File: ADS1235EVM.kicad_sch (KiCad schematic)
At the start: 60 parts, among them J1 Conn_01x04_Pin, J2 Conn_01x11_Pin, U1 ADS1235QWRHMRQ1, U2 LM27762, U5 UCC27524DGN

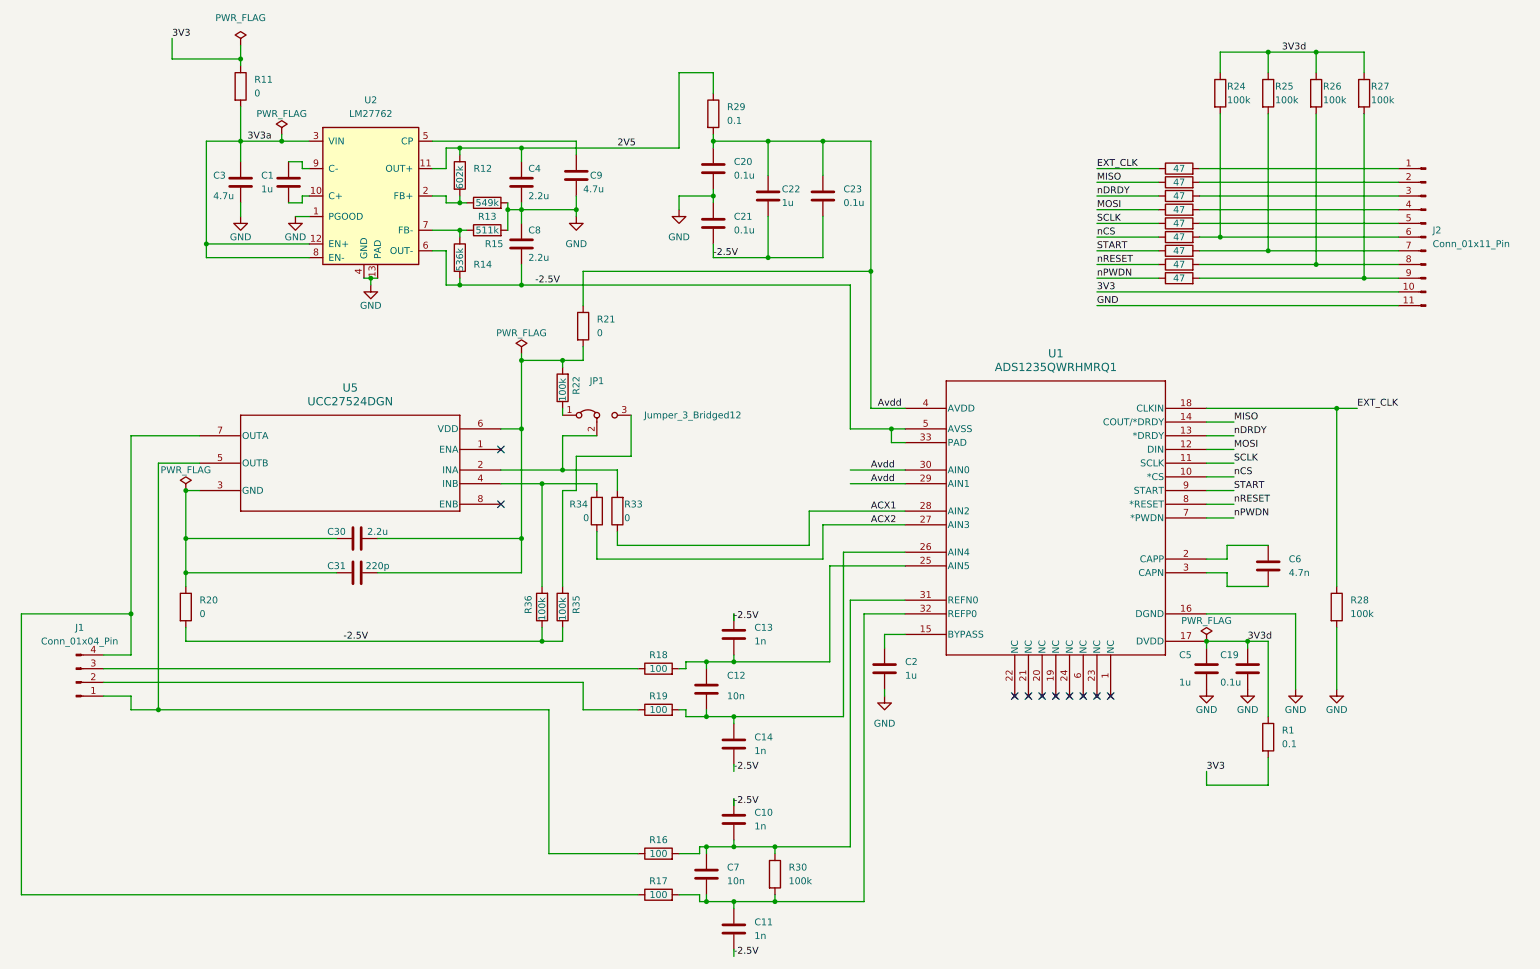
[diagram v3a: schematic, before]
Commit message: Add of 2.54mm SPI connector & open jumper
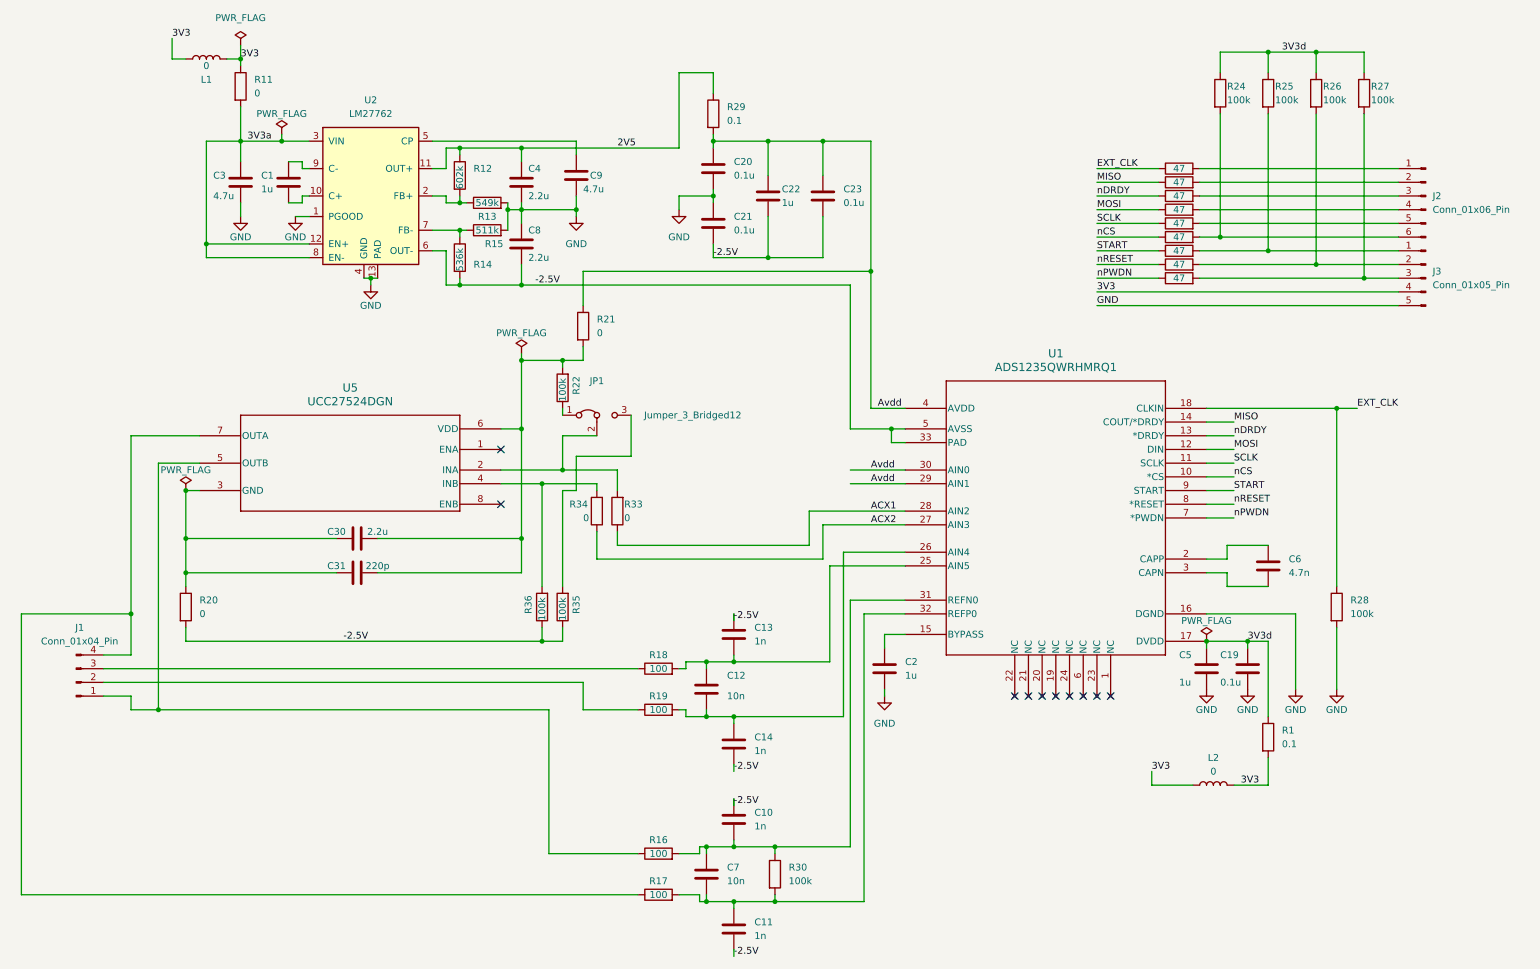
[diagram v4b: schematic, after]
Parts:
- removed J2: Conn_01x11_Pin, Connector_PinHeader_1.27mm:PinHeader_1x11_P1.27mm_Vertical, symbol Connector:Conn_01x11_Pin
- added J2: Conn_01x06_Pin, Connector_PinHeader_2.54mm:PinHeader_1x06_P2.54mm_Vertical, symbol Connector:Conn_01x06_Pin
- added J3: Conn_01x05_Pin, Connector_PinHeader_2.54mm:PinHeader_1x05_P2.54mm_Vertical, symbol Connector:Conn_01x05_Pin
- added L1, L2: 0, Inductor_SMD:L_0402_1005Metric, symbol Device:L
- J1: footprint Connector_Hirose:Hirose_DF13-04P-1.25DS_1x04_P1.25mm_Horizontal -> Connector_Hirose:Hirose_DF13-04P-1.25DSA_1x04_P1.25mm_Vertical
- JP1: footprint Jumper:SolderJumper-3_P1.3mm_Bridged12_RoundedPad1.0x1.5mm -> Jumper:SolderJumper-3_P1.3mm_Open_RoundedPad1.0x1.5mm
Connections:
- net 3V3: now also J3.4 (Pin_4), L1.1, L1.2, L2.1, L2.2
- net GND: now also J3.5 (Pin_5)
- net at R26.2, R8.2: now also J3.2 (Pin_2)
- net at R10.2, R27.2: now also J3.3 (Pin_3)
- net at R25.2, R9.2: now also J3.1 (Pin_1)
- net at R24.2, R6.2: now also J2.6 (Pin_6)
- net at R4.2: now also J2.4 (Pin_4)
- net at R3.2: now also J2.2 (Pin_2)
- net at R5.2: now also J2.5 (Pin_5)
- net at R7.2: now also J2.1 (Pin_1)
- net at R2.2: now also J2.3 (Pin_3)
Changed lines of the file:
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@@
     (stroke (width 0) (type default))
   )
-  (wire (pts (xy 236.22 156.21) (xy 247.65 156.21))
+  (wire (pts (xy 241.3 156.21) (xy 247.65 156.21))
     (stroke (width 0) (type default))
   )
@@
     (stroke (width 0) (type default))
   )
-  (wire (pts (xy 236.22 153.67) (xy 236.22 156.21))
-    (stroke (width 0) (type default))
-  )
   (wire (pts (xy 95.25 38.1) (xy 97.79 38.1))
     (stroke (width 0) (type default))
@@
     (stroke (width 0) (type default))
   )
+  (wire (pts (xy 226.06 153.67) (xy 226.06 156.21))
+    (stroke (width 0) (type default))
+  )
   (wire (pts (xy 236.22 116.84) (xy 240.03 116.84))
     (stroke (width 0) (type default))
@@
     (stroke (width 0) (type default))
   )
+  (wire (pts (xy 46.99 21.59) (xy 44.45 21.59))
+    (stroke (width 0) (type default))
+  )
   (wire (pts (xy 109.22 90.17) (xy 109.22 110.49))
     (stroke (width 0) (type default))
@@
     (stroke (width 0) (type default))
   )
+  (wire (pts (xy 233.68 156.21) (xy 226.06 156.21))
+    (stroke (width 0) (type default))
+  )
   (wire (pts (xy 97.79 38.1) (xy 109.22 38.1))
     (stroke (width 0) (type default))
@@
     (stroke (width 0) (type default))
   )
-  (wire (pts (xy 57.15 21.59) (xy 44.45 21.59))
+  (wire (pts (xy 57.15 21.59) (xy 54.61 21.59))
     (stroke (width 0) (type default))
   )
@@
     (effects (font (size 1.27 1.27)) (justify left bottom))
   )
-  (label "3V3" (at 236.22 153.67 0) (fields_autoplaced)
+  (label "3V3" (at 242.57 156.21 0) (fields_autoplaced)
+    (effects (font (size 1.27 1.27)) (justify left bottom))
+  )
+  (label "3V3" (at 226.06 153.67 0) (fields_autoplaced)
+    (effects (font (size 1.27 1.27)) (justify left bottom))
+  )
+  (label "3V3" (at 57.15 21.59 0) (fields_autoplaced)
     (effects (font (size 1.27 1.27)) (justify left bottom))
   )
@@
         (path "/eda615d8-e9fe-47dd-8aa4-13a32693ef53"
           (reference "R26") (unit 1)
+        )
+      )
+    )
+  )
+  (symbol (lib_id "Connector:Conn_01x06_Pin") (at 276.86 46.99 0) (mirror y) (unit 1)
+    (in_bom yes) (on_board yes) (dnp no) (fields_autoplaced)
+    (property "Reference" "J2" (at 278.13 46.99 0)
+      (effects (font (size 1.27 1.27)) (justify right))
+    )
+    (property "Value" "Conn_01x06_Pin" (at 278.13 49.53 0)
+      (effects (font (size 1.27 1.27)) (justify right))
+    )
+    (property "Footprint" "Connector_PinHeader_2.54mm:PinHeader_1x06_P2.54mm_Vertical" (at 276.86 46.99 0)
+      (effects (font (size 1.27 1.27)) hide)
+    )
+    (property "Datasheet" "~" (at 276.86 46.99 0)
+      (effects (font (size 1.27 1.27)) hide)
+    )
+    (pin "1")
+    (pin "2")
+    (pin "3")
+    (pin "4")
+    (pin "5")
+    (pin "6")
+    (instances
+      (project "ADS1235EVM"
+        (path "/4faaba4a-da34-4767-a6c4-a9ccb9f4f95a"
+          (reference "J2") (unit 1)
         )
       )
@@
     )
   )
+  (symbol (lib_id "Device:L") (at 50.8 21.59 90) (unit 1)
+    (in_bom yes) (on_board yes) (dnp no)
+    (property "Reference" "L1" (at 50.8 25.4 90)
+      (effects (font (size 1.27 1.27)))
+    )
+    (property "Value" "0" (at 50.8 22.86 90)
+      (effects (font (size 1.27 1.27)))
+    )
+    (property "Footprint" "Inductor_SMD:L_0402_1005Metric" (at 50.8 21.59 0)
+      (effects (font (size 1.27 1.27)) hide)
+    )
+    (property "Datasheet" "~" (at 50.8 21.59 0)
+      (effects (font (size 1.27 1.27)) hide)
+    )
+    (pin "1")
+    (pin "2")
+    (instances
+      (project "ADS1235EVM"
+        (path "/4faaba4a-da34-4767-a6c4-a9ccb9f4f95a"
+          (reference "L1") (unit 1)
+        )
+      )
+    )
+  )
   (symbol (lib_id "Device:C") (at 144.78 41.91 0) (unit 1)
     (in_bom yes) (on_board yes) (dnp no) (fields_autoplaced)
@@
       (effects (font (size 1.27 1.27)))
     )
-    (property "Footprint" "Jumper:SolderJumper-3_P1.3mm_Bridged12_RoundedPad1.0x1.5mm" (at 123.19 87.63 0)
+    (property "Footprint" "Jumper:SolderJumper-3_P1.3mm_Open_RoundedPad1.0x1.5mm" (at 123.19 87.63 0)
       (effects (font (size 1.27 1.27)) hide)
     )
@@
     )
   )
+  (symbol (lib_id "Device:L") (at 237.49 156.21 90) (unit 1)
+    (in_bom yes) (on_board yes) (dnp no) (fields_autoplaced)
+    (property "Reference" "L2" (at 237.49 151.13 90)
+      (effects (font (size 1.27 1.27)))
+    )
+    (property "Value" "0" (at 237.49 153.67 90)
+      (effects (font (size 1.27 1.27)))
+    )
+    (property "Footprint" "Inductor_SMD:L_0402_1005Metric" (at 237.49 156.21 0)
+      (effects (font (size 1.27 1.27)) hide)
+    )
+    (property "Datasheet" "~" (at 237.49 156.21 0)
+      (effects (font (size 1.27 1.27)) hide)
+    )
+    (pin "1")
+    (pin "2")
+    (instances
+      (project "ADS1235EVM"
+        (path "/4faaba4a-da34-4767-a6c4-a9ccb9f4f95a"
+          (reference "L2") (unit 1)
+        )
+      )
+    )
+  )
   (symbol (lib_id "Device:R") (at 57.15 26.67 0) (unit 1)
     (in_bom yes) (on_board yes) (dnp no) (fields_autoplaced)
@@
     )
   )
+  (symbol (lib_id "Connector:Conn_01x05_Pin") (at 276.86 62.23 0) (mirror y) (unit 1)
+    (in_bom yes) (on_board yes) (dnp no) (fields_autoplaced)
+    (property "Reference" "J3" (at 278.13 60.96 0)
+      (effects (font (size 1.27 1.27)) (justify right))
+    )
+    (property "Value" "Conn_01x05_Pin" (at 278.13 63.5 0)
+      (effects (font (size 1.27 1.27)) (justify right))
+    )
+    (property "Footprint" "Connector_PinHeader_2.54mm:PinHeader_1x05_P2.54mm_Vertical" (at 276.86 62.23 0)
+      (effects (font (size 1.27 1.27)) hide)
+    )
+    (property "Datasheet" "~" (at 276.86 62.23 0)
+      (effects (font (size 1.27 1.27)) hide)
+    )
+    (pin "1")
+    (pin "2")
+    (pin "3")
+    (pin "4")
+    (pin "5")
+    (instances
+      (project "ADS1235EVM"
+        (path "/4faaba4a-da34-4767-a6c4-a9ccb9f4f95a"
+          (reference "J3") (unit 1)
+        )
+      )
+    )
+  )
   (symbol (lib_id "power:PWR_FLAG") (at 64.77 35.56 0) (unit 1)
     (in_bom yes) (on_board yes) (dnp no)
@@
   )
   (symbol (lib_id "power:PWR_FLAG") (at 57.15 19.05 0) (unit 1)
-    (in_bom yes) (on_board yes) (dnp no) (fields_autoplaced)
+    (in_bom yes) (on_board yes) (dnp no)
     (property "Reference" "#FLG02" (at 57.15 17.145 0)
       (effects (font (size 1.27 1.27)) hide)
@@
     )
   )
-  (symbol (lib_id "Connector:Conn_01x11_Pin") (at 276.86 54.61 0) (mirror y) (unit 1)
-    (in_bom yes) (on_board yes) (dnp no) (fields_autoplaced)
-    (property "Reference" "J2" (at 278.13 53.34 0)
-      (effects (font (size 1.27 1.27)) (justify right))
-    )
-    (property "Value" "Conn_01x11_Pin" (at 278.13 55.88 0)
-      (effects (font (size 1.27 1.27)) (justify right))
-    )
-    (property "Footprint" "Connector_PinHeader_1.27mm:PinHeader_1x11_P1.27mm_Vertical" (at 276.86 54.61 0)
-      (effects (font (size 1.27 1.27)) hide)
-    )
-    (property "Datasheet" "~" (at 276.86 54.61 0)
-      (effects (font (size 1.27 1.27)) hide)
-    )
-    (pin "1")
-    (pin "10")
-    (pin "11")
-    (pin "2")
-    (pin "3")
-    (pin "4")
-    (pin "5")
-    (pin "6")
-    (pin "7")
-    (pin "8")
-    (pin "9")
-    (instances
-      (project "ADS1235EVM"
-        (path "/4faaba4a-da34-4767-a6c4-a9ccb9f4f95a"
-          (reference "J2") (unit 1)
-        )
-      )
-    )
-  )
   (symbol (lib_id "Device:C") (at 148.59 162.56 0) (unit 1)
     (in_bom yes) (on_board yes) (dnp no) (fields_autoplaced)
@@
       (effects (font (size 1.27 1.27)))
     )
-    (property "Footprint" "Connector_Hirose:Hirose_DF13-04P-1.25DS_1x04_P1.25mm_Horizontal" (at 26.67 134.62 0)
-      (effects (font (size 1.27 1.27)) hide)
-    )
+    (property "Footprint" "Connector_Hirose:Hirose_DF13-04P-1.25DSA_1x04_P1.25mm_Vertical" (at 26.67 134.62 0)
+      (effects (font (size 1.27 1.27)) hide)
+    )

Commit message: KiCAD - Change ferrite net names
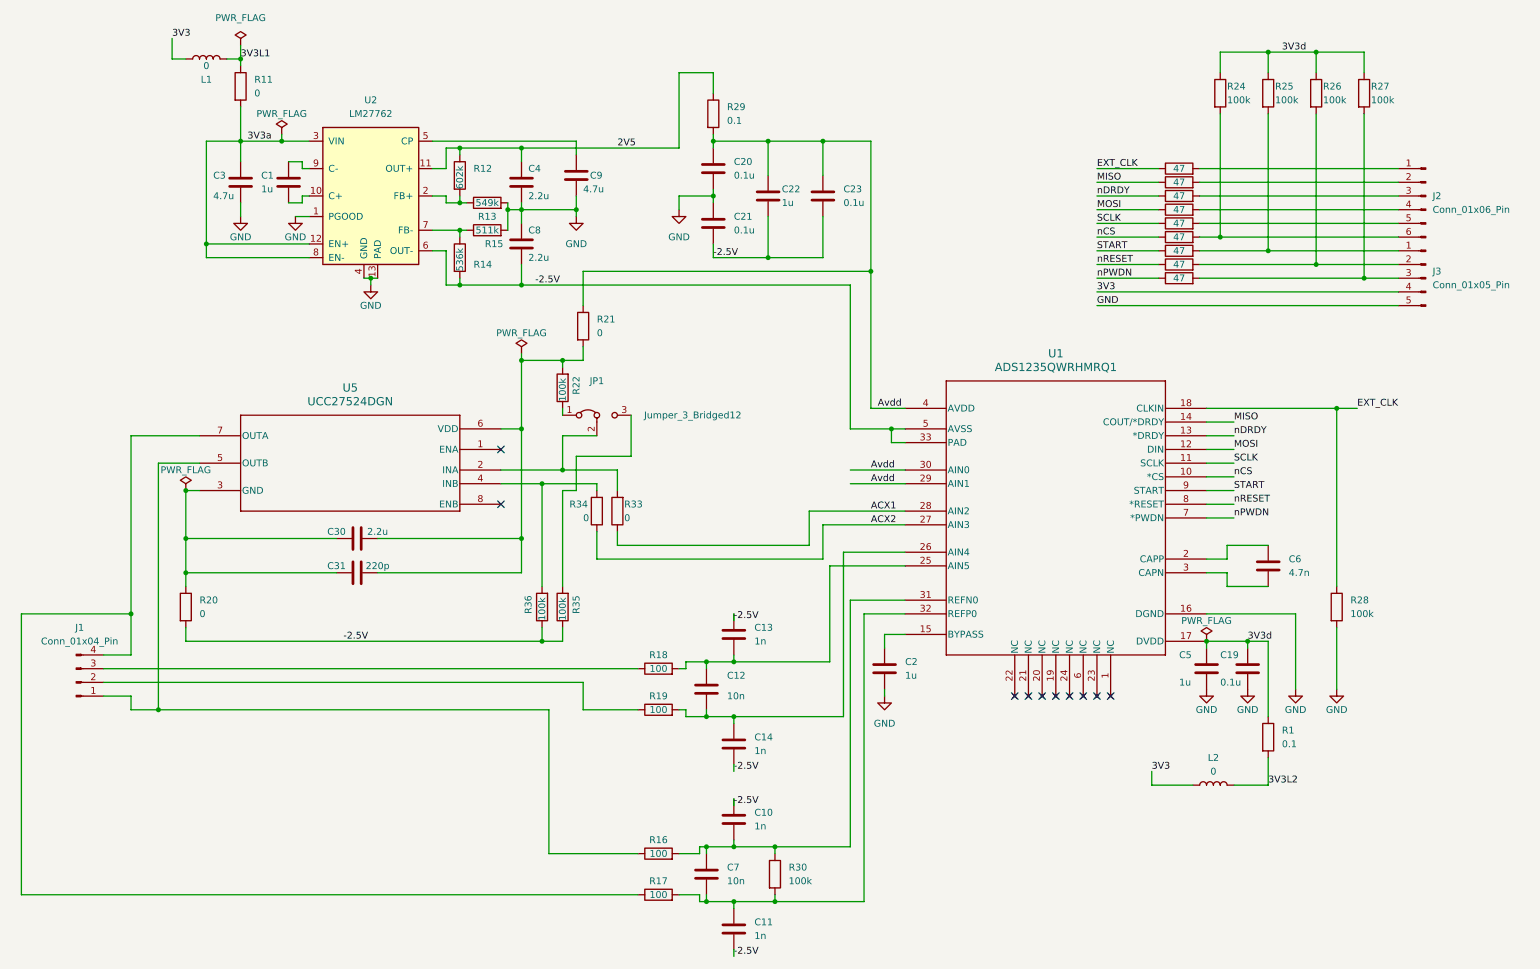
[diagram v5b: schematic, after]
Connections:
- net 3V3: no longer L1.2, L2.2, R1.2, R11.1
- new net 3V3L1: L1.2, R11.1
- new net 3V3L2: L2.2, R1.2
